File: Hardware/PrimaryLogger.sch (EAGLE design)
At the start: 91 parts, among them J1 CONN_42.54_SCREW, J2 CONN_42.54_SCREW, J3 CONN_42.54_SCREW, J4 CONN_42.54_SCREW, J5 CONN_32.54_SCREW, J9 GEMS_POWER_PLUGINPUT, Q1 DMG3404, Q2 DMG3404, U1 MCP7940SOIC, U10 PCA9617TSSOP8, U11 SN74AUP3G34DCU, U12 SN74LVC1G3157SC70, U2 TPL5010DDC, U3 MCP23008SSOP, U4 SHTC3DFN, U5 TCS3400, U6 TPL5010DDC, U7 MIC2005, U8 MIC2005, U9 MIC842

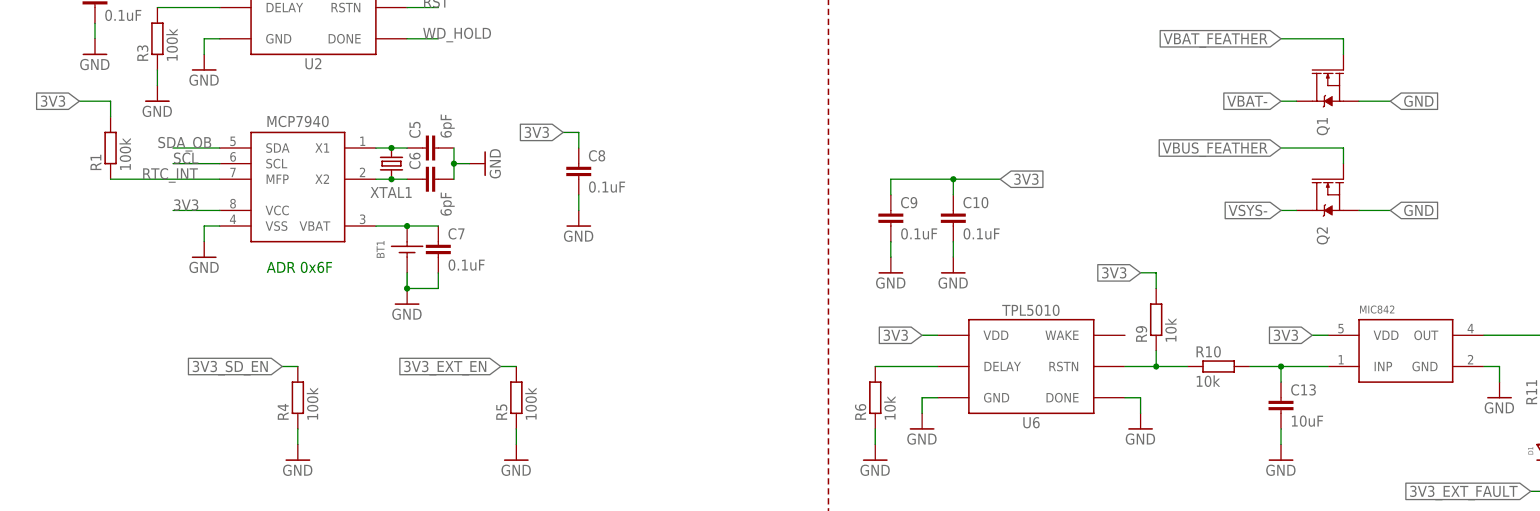
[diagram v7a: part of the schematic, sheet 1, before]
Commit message: Updated part values for BoM generation
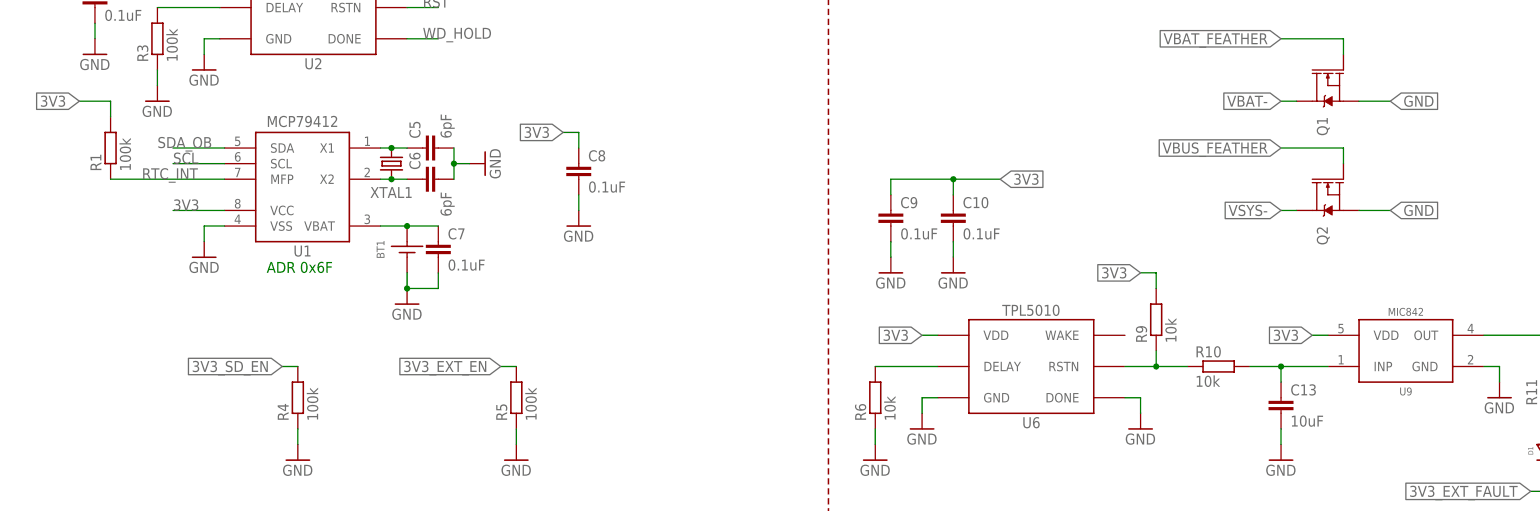
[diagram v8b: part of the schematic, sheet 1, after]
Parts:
- D1: value LED0603 -> LEDRED0603; device bschulz:LED0603 -> bschulz:LEDRED0603
- D2: value LED0603 -> LEDGREEN0603; device bschulz:LED0603 -> bschulz:LEDGREEN0603
- R14: value 100k -> 10k
- R16, R2: device bschulz_passives:R-EU_R0603 -> bschulz_passives:R-EU_0.0R0603
- R19, R20, R23, R24: value (none) -> 4.7k
- U1: value MCP7940SOIC -> MCP79412SOIC; device bschulz:MCP7940SOIC -> bschulz:MCP79412SOIC
- U9: value MIC842 -> MIC842L; device bschulz:MIC842 -> bschulz:MIC842L
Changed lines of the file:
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@@
 </classes>
 <parts>
-<part name="U1" library="bschulz" deviceset="MCP7940" device="SOIC"/>
+<part name="U1" library="bschulz" deviceset="MCP794*" device="SOIC" technology="12" value="MCP79412SOIC"/>
 <part name="XTAL1" library="bschulz" deviceset="CRYSTAL" device="3.2X1.5">
 <attribute name="DIGIKEY" value="535-11937-1-ND"/>
@@
 <part name="J5" library="bschulz" deviceset="CONN_3" device="2.54_SCREW"/>
 <part name="J8" library="bschulz" deviceset="CONN_02" device="2.54_SCREW_ROUND"/>
-<part name="R14" library="bschulz_passives" deviceset="R-EU_" device="R0603" technology="10K" value="100k"/>
+<part name="R14" library="bschulz_passives" deviceset="R-EU_" device="R0603" technology="10K" value="10k"/>
 <part name="J6" library="bschulz" deviceset="CONN_02" device="3.5MM_ROUND"/>
 <part name="J7" library="bschulz" deviceset="CONN_02" device="3.5MM_ROUND"/>
@@
 <part name="GND24" library="supply1" library_urn="urn:adsk.eagle:library:371" deviceset="GND" device=""/>
 <part name="U6" library="bschulz" deviceset="TPL5010" device="DDC"/>
-<part name="U9" library="bschulz" deviceset="MIC842" device=""/>
+<part name="U9" library="bschulz" deviceset="MIC842" device="" technology="L" value="MIC842L"/>
 <part name="GND25" library="supply1" library_urn="urn:adsk.eagle:library:371" deviceset="GND" device=""/>
 <part name="GND26" library="supply1" library_urn="urn:adsk.eagle:library:371" deviceset="GND" device=""/>
@@
 <part name="R11" library="bschulz_passives" deviceset="R-EU_" device="R0603" technology="4.7K" value="4.7k"/>
 <part name="R12" library="bschulz_passives" deviceset="R-EU_" device="R0603" technology="4.7K" value="4.7k"/>
-<part name="D1" library="bschulz" deviceset="LED" device="0603"/>
-<part name="D2" library="bschulz" deviceset="LED" device="0603"/>
+<part name="D1" library="bschulz" deviceset="LED" device="0603" technology="RED" value="LEDRED0603"/>
+<part name="D2" library="bschulz" deviceset="LED" device="0603" technology="GREEN" value="LEDGREEN0603"/>
 <part name="GND30" library="supply1" library_urn="urn:adsk.eagle:library:371" deviceset="GND" device=""/>
 <part name="C9" library="bschulz_passives" deviceset="C-EU" device="C0603" technology="0.1UF" value="0.1uF"/>
@@
 <part name="GND34" library="supply1" library_urn="urn:adsk.eagle:library:371" deviceset="GND" device=""/>
 <part name="GND35" library="supply1" library_urn="urn:adsk.eagle:library:371" deviceset="GND" device=""/>
-<part name="R19" library="bschulz_passives" deviceset="R-EU_" device="R0603" technology="4.7K"/>
-<part name="R20" library="bschulz_passives" deviceset="R-EU_" device="R0603" technology="4.7K"/>
-<part name="R23" library="bschulz_passives" deviceset="R-EU_" device="R0603" technology="4.7K"/>
-<part name="R24" library="bschulz_passives" deviceset="R-EU_" device="R0603" technology="4.7K"/>
+<part name="R19" library="bschulz_passives" deviceset="R-EU_" device="R0603" technology="4.7K" value="4.7k"/>
+<part name="R20" library="bschulz_passives" deviceset="R-EU_" device="R0603" technology="4.7K" value="4.7k"/>
+<part name="R23" library="bschulz_passives" deviceset="R-EU_" device="R0603" technology="4.7K" value="4.7k"/>
+<part name="R24" library="bschulz_passives" deviceset="R-EU_" device="R0603" technology="4.7K" value="4.7k"/>
 <part name="U3" library="bschulz" deviceset="MCP23008" device="SSOP"/>
 <part name="GND36" library="supply1" library_urn="urn:adsk.eagle:library:371" deviceset="GND" device=""/>
@@
 <part name="GND37" library="supply1" library_urn="urn:adsk.eagle:library:371" deviceset="GND" device=""/>
 <part name="GND38" library="supply1" library_urn="urn:adsk.eagle:library:371" deviceset="GND" device=""/>
-<part name="R2" library="bschulz_passives" deviceset="R-EU_" device="R0603" value="0R"/>
-<part name="R16" library="bschulz_passives" deviceset="R-EU_" device="R0603" value="0R"/>
+<part name="R2" library="bschulz_passives" deviceset="R-EU_" device="R0603" technology="0.0" value="0R"/>
+<part name="R16" library="bschulz_passives" deviceset="R-EU_" device="R0603" technology="0.0" value="0R"/>
 </parts>
 <sheets>
@@
 </plain>
 <instances>
-<instance part="U1" gate="G$1" x="50.8" y="106.68" smashed="yes"/>
+<instance part="U1" gate="G$1" x="54.102" y="106.68" smashed="yes">
+<attribute name="DISP" x="54.102" y="116.078" size="1.778" layer="95" align="center"/>
+<attribute name="NAME" x="54.102" y="94.996" size="1.778" layer="95" ratio="15" align="center"/>
+</instance>
 <instance part="XTAL1" gate="G$1" x="68.58" y="109.22" smashed="yes" rot="R270">
 <attribute name="NAME" x="68.58" y="103.632" size="1.778" layer="95" font="vector" align="bottom-center"/>
@@
 <attribute name="NAME" x="172.72" y="67.056" size="1.778" layer="95" ratio="15" align="center"/>
 </instance>
-<instance part="U9" gate="G$1" x="231.14" y="78.74" smashed="yes"/>
+<instance part="U9" gate="G$1" x="231.14" y="78.74" smashed="yes">
+<attribute name="NAME" x="233.68" y="72.136" size="1.27" layer="95" ratio="15" align="center"/>
+</instance>
 <instance part="GND25" gate="1" x="154.94" y="66.04" smashed="yes">
 <attribute name="VALUE" x="152.4" y="63.5" size="1.778" layer="96"/>
@@
 <pinref part="U1" gate="G$1" pin="X1"/>
 <pinref part="XTAL1" gate="G$1" pin="1"/>
-<wire x1="66.04" y1="111.76" x2="68.58" y2="111.76" width="0.1524" layer="91"/>
+<wire x1="66.802" y1="111.76" x2="68.58" y2="111.76" width="0.1524" layer="91"/>
 <pinref part="C5" gate="G$1" pin="1"/>
 <wire x1="68.58" y1="111.76" x2="71.12" y2="111.76" width="0.1524" layer="91"/>
@@
 <pinref part="U1" gate="G$1" pin="X2"/>
 <pinref part="XTAL1" gate="G$1" pin="2"/>
-<wire x1="66.04" y1="106.68" x2="68.58" y2="106.68" width="0.1524" layer="91"/>
+<wire x1="66.802" y1="106.68" x2="68.58" y2="106.68" width="0.1524" layer="91"/>
 <pinref part="C6" gate="G$1" pin="1"/>
 <wire x1="68.58" y1="106.68" x2="71.12" y2="106.68" width="0.1524" layer="91"/>
@@
 <segment>
 <pinref part="U1" gate="G$1" pin="VSS"/>
-<wire x1="40.64" y1="99.06" x2="38.1" y2="99.06" width="0.1524" layer="91"/>
+<wire x1="41.402" y1="99.06" x2="38.1" y2="99.06" width="0.1524" layer="91"/>
 <wire x1="38.1" y1="99.06" x2="38.1" y2="96.52" width="0.1524" layer="91"/>
 <pinref part="GND3" gate="1" pin="GND"/>
@@
 <segment>
 <pinref part="U1" gate="G$1" pin="SCL"/>
-<wire x1="40.64" y1="109.22" x2="33.02" y2="109.22" width="0.1524" layer="91"/>
+<wire x1="41.402" y1="109.22" x2="33.02" y2="109.22" width="0.1524" layer="91"/>
 <label x="33.02" y="109.22" size="1.778" layer="95"/>
 </segment>
@@
 <label x="27.94" y="106.68" size="1.778" layer="95"/>
 <pinref part="R1" gate="G$1" pin="1"/>
-<wire x1="22.86" y1="106.68" x2="40.64" y2="106.68" width="0.1524" layer="91"/>
+<wire x1="22.86" y1="106.68" x2="41.402" y2="106.68" width="0.1524" layer="91"/>
 </segment>
 </net>
@@
 <pinref part="BT1" gate="G$1" pin="+"/>
 <pinref part="U1" gate="G$1" pin="VBAT"/>
-<wire x1="71.12" y1="99.06" x2="66.04" y2="99.06" width="0.1524" layer="91"/>
+<wire x1="71.12" y1="99.06" x2="66.802" y2="99.06" width="0.1524" layer="91"/>
 <pinref part="C7" gate="G$1" pin="1"/>
 <wire x1="76.2" y1="99.06" x2="71.12" y2="99.06" width="0.1524" layer="91"/>
@@
 <segment>
 <pinref part="U1" gate="G$1" pin="VCC"/>
-<wire x1="40.64" y1="101.6" x2="33.02" y2="101.6" width="0.1524" layer="91"/>
+<wire x1="41.402" y1="101.6" x2="33.02" y2="101.6" width="0.1524" layer="91"/>
 <label x="33.02" y="101.6" size="1.778" layer="95"/>
 </segment>
@@
 <segment>
 <pinref part="U1" gate="G$1" pin="SDA"/>
-<wire x1="40.64" y1="111.76" x2="33.02" y2="111.76" width="0.1524" layer="91"/>
+<wire x1="41.402" y1="111.76" x2="33.02" y2="111.76" width="0.1524" layer="91"/>
 <label x="30.48" y="111.76" size="1.778" layer="95"/>
 </segment>
